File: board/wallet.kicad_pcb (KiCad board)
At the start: 4 copper layers, 48 x 85 mm, 136 parts, among them J1 TYPE-C-31-M-12, U1 BQ25185DLHR, U10 SN74LVC1T45DBVR, U11 E73-2G4M08S1C, U12 ME6211C28M5G-N, U13 TPS60230RGTR, U14 TLV75801PDBVR, U15 MAX17048G+T10, U2 TPS63802DLAR, U3 XC6206P332MR-G, U4 STM32U585VIT6Q, U5 SE050E2HQ1/Z01Z3Z, U6 TS3USB221ARSER, U7 SN74LVC1G02DBVR(UMW), U8 TPS22917DBVR, U9 SN74LVC1T45DBVR, Y1 Q13FC13500049

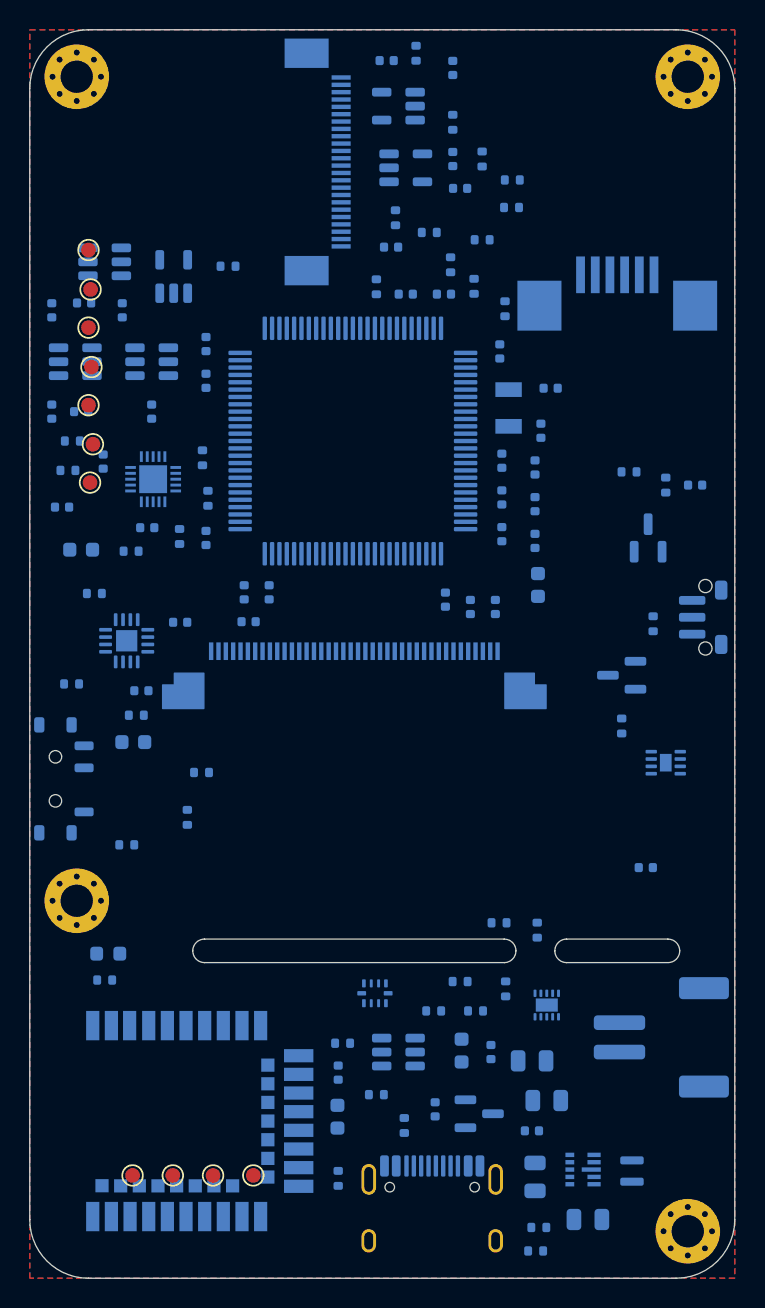
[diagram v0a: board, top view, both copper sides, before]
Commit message: Owner's hand placement and first routing
43 parts re-placed by hand (charger and buck-boost clusters tightened around
U1/U2 in the chin, battery gauge moved next to the MCU's I2C, decoupling and
crystal caps pulled in against their pins) and 38 nets routed: the power
chain, USB, display SPI, LSE, I2C, radio SWD, charger control.
310 track segments, 31 vias.

Co-Authored-By: Claude Opus 5.5 <noreply@anthropic.com>
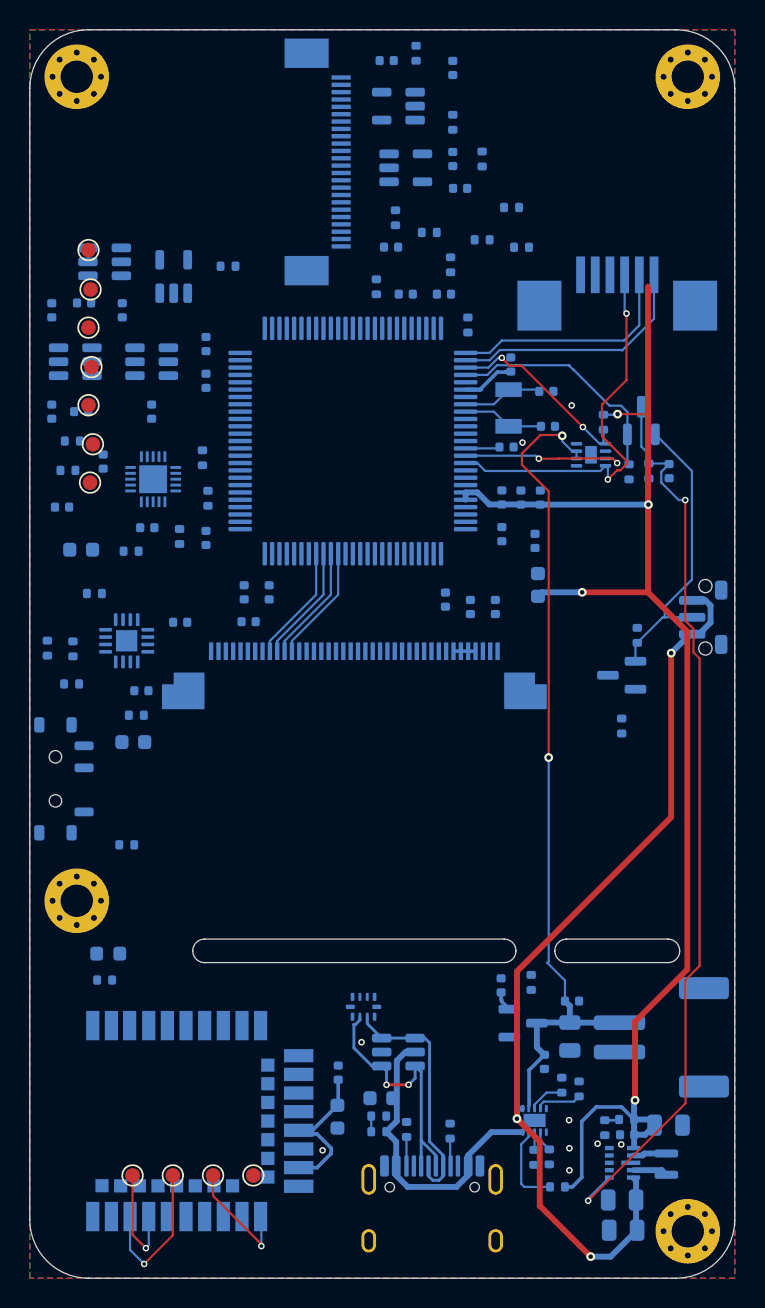
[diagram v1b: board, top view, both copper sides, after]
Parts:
- moved U15 21.6 mm to (38.2, 28.9)
- moved R_AIRS 15.0 mm to (1.20, 42.1)
- moved R_STAT1 14.6 mm to (35.9, 78.8), turned to 0 degrees
- moved R_ILIM 13.4 mm to (35.4, 76.7), turned to -90 degrees
- moved C_SYS 13.1 mm to (40.4, 81.7)
- moved R_ALRT 12.8 mm to (39.1, 26.7)
- moved R_CE 12.6 mm to (37.4, 72.1), turned to 90 degrees
- moved R_BLEN 12.1 mm to (2.94, 42.1), turned to 90 degrees
- moved C_USBSW 10.8 mm to (40.7, 75.2), turned to 180 degrees
- moved R_ISET 10.7 mm to (34.3, 76.8), turned to -90 degrees
- moved R_STAT2 10.7 mm to (36.2, 71.8)
- moved C_GAUGE 10.4 mm to (36.9, 66.1)
- moved C_RTC 10.1 mm to (32.1, 65.1), turned to 90 degrees
- moved R_FB2 9.62 mm to (39.1, 74.8), turned to -90 degrees
- moved R_FB1 9.47 mm to (40.6, 74.2), turned to 180 degrees
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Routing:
- net V3V3: track 0.00 -> 98.0 mm, vias 0 -> 4
- net PWR_EN: track 0.00 -> 62.5 mm, vias 0 -> 2
- net SYS: track 0.00 -> 62.1 mm, vias 0 -> 3
- net BAT: track 0.00 -> 57.5 mm, vias 0 -> 2
- net I2C_SDA: track 0.00 -> 26.9 mm, vias 0 -> 2
- net VBUS: track 0.00 -> 21.1 mm
- net BTN: track 0.00 -> 20.2 mm
- net USB_DP: track 0.00 -> 18.3 mm, vias 0 -> 2
- net USB_DN: track 0.00 -> 17.0 mm
- net CTP_INT: track 0.00 -> 17.0 mm
- net CTP_RST: track 0.00 -> 17.0 mm
- net PWR_HOLD: track 0.00 -> 16.2 mm
- net GAUGE_ALRT: track 0.00 -> 13.2 mm, vias 0 -> 2
- net I2C_SCL: track 0.00 -> 11.5 mm, vias 0 -> 2
- net RADIO_SWCLK: track 0.00 -> 10.5 mm, vias 0 -> 1
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
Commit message: Pre-route block wiring around the owner's routing; fix the stale MCU pin table
- board: block wiring (each IC and its passives) and GND fanouts routed with
  humanizedKicadAutoRouter on top of the owner's copper, which stays fixed;
  the USB pair from the MCU to the USB switch is routed first. The camera bus
  and VDD11's cross-package link are left to the human, like all wiring
  between blocks. 341/341 owner items and every footprint position unchanged;
  DRC has no new items, 10 of 12 starved thermals fixed. Autorouting the
  remainder as a judge: 2 failed nets (camera knot) vs 5 before.
- mcuAssign.json said USART1/PA9-PA10 for the radio but the netlist was never
  re-exported, so the board kept USART3/PB10-PB11. USART1 trial-routed worse
  (4 vs 2 failed), so the table now matches the board; checkMcuAf.py also
  fails when the table and the exported netlist disagree.
- scripts/partialRoute.py (new): partial routing with existing copper fixed,
  --first-nets, --skip-nets, --max-mm, --leave-under; removes its own
  dangling stubs.
- scripts/placeLoop.py (new): locked optimize -> partial route -> KRT judge.
- optimizePlacement: courtyards may touch, decap-to-pin cost, locked parts,
  clearance to existing copper. optimizePins: --keep-routed, --only, --out.
- checkDensity.py retired: the owner's placement packs courtyards touching.

Co-Authored-By: Claude Opus 5.5 <noreply@anthropic.com>
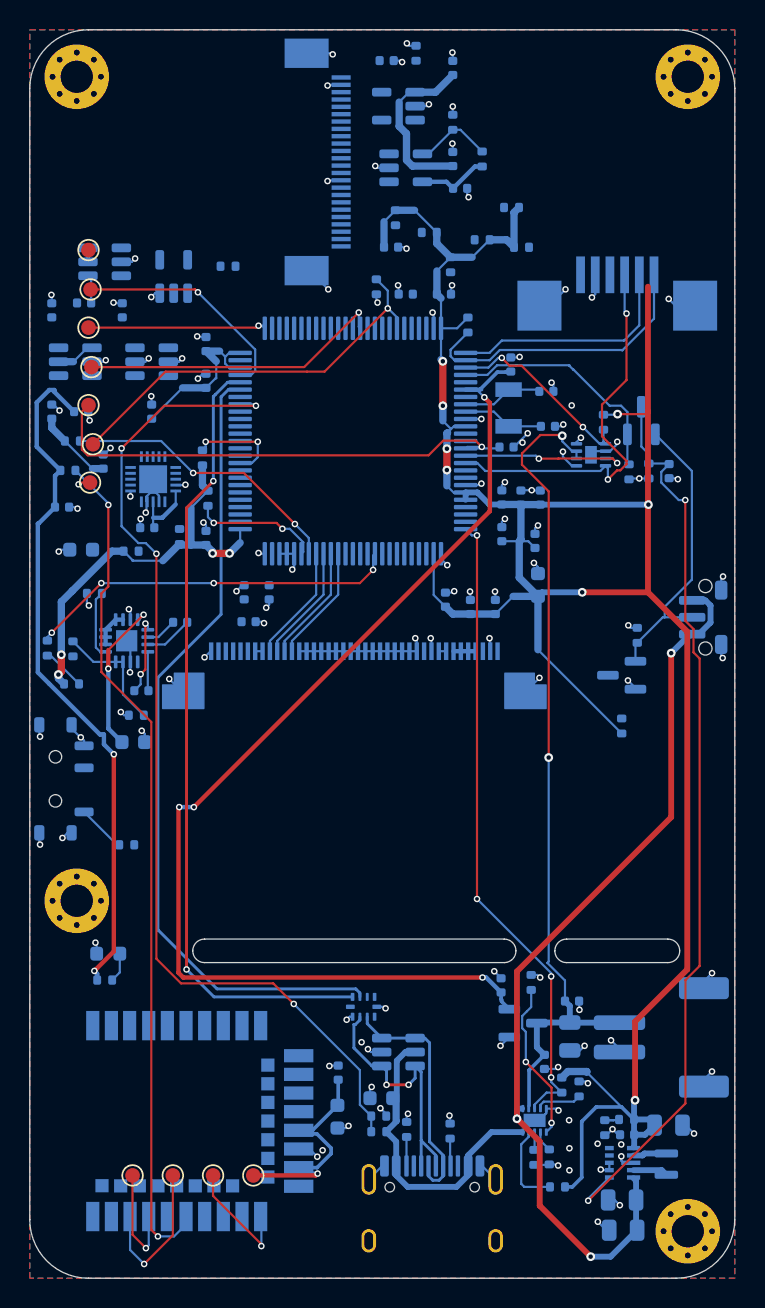
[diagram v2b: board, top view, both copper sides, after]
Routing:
- net V3V3: track 98.0 -> 236.9 mm, vias 4 -> 12
- net GND: track 0.00 -> 119.8 mm, vias 9 -> 123
- net VBAT_RTC: track 6.04 -> 78.7 mm, vias 0 -> 4
- net VBUS_SENSE: track 1.06 -> 69.0 mm, vias 0 -> 4
- net RADIO_TX: track 0.00 -> 57.7 mm, vias 0 -> 2
- net USB_DN_MCU: track 0.00 -> 55.4 mm
- net USB_DP_MCU: track 0.00 -> 54.1 mm, vias 0 -> 2
- net RADIO_3V3: track 10.1 -> 64.1 mm, vias 0 -> 3
- net CHG_STAT2: track 2.71 -> 44.0 mm, vias 0 -> 4
- net NRST: track 2.34 -> 34.7 mm, vias 0 -> 1
- net BOOT0: track 0.00 -> 27.8 mm, vias 0 -> 1
- net AIRGAP_SENSE: track 0.00 -> 25.5 mm, vias 0 -> 4
- net SWO: track 0.00 -> 20.9 mm, vias 0 -> 1
- net RADIO_TXD_MCU: track 0.00 -> 19.4 mm, vias 0 -> 2
- net SWDIO: track 0.00 -> 15.5 mm, vias 0 -> 1
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
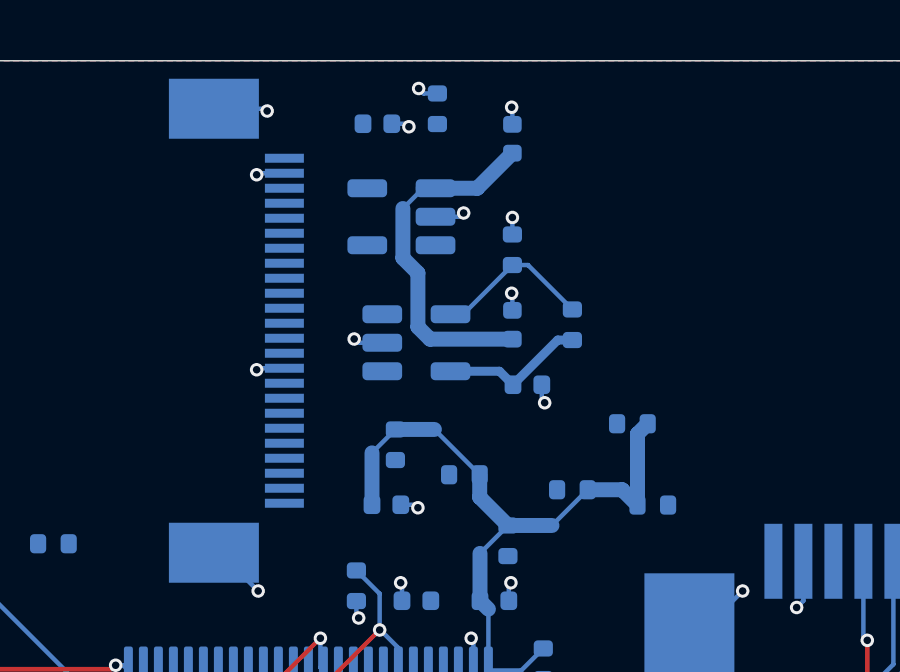
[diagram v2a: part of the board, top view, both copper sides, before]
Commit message: Owner's fixes on the pre-routed board (checkpoint before rework)
Co-Authored-By: Claude Opus 5.5 <noreply@anthropic.com>
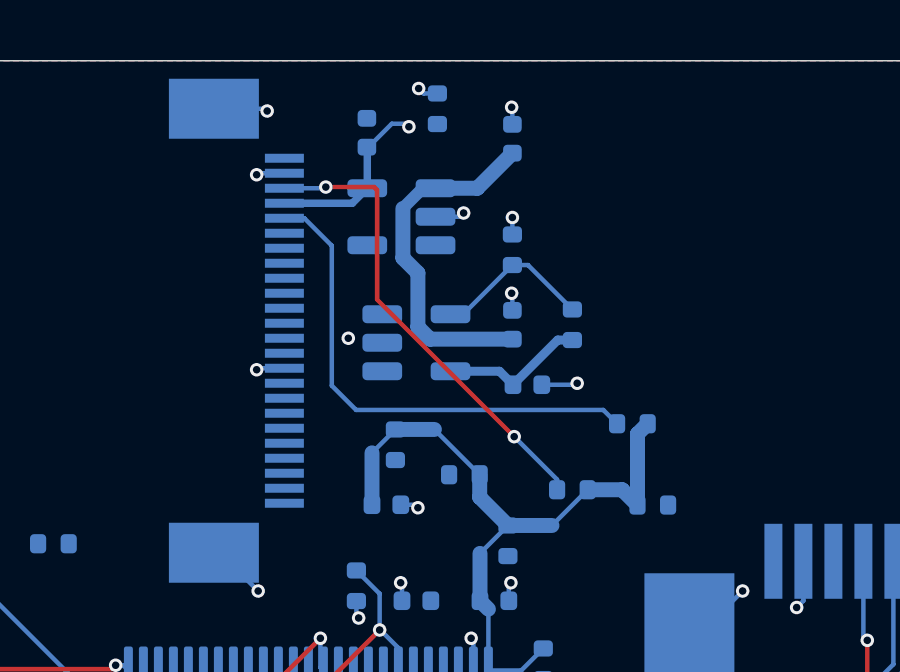
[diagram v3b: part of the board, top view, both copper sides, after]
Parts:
- moved C_AVOUT 0.46 mm to (23.9, 2.40), turned to 90 degrees
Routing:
- net CAM_SCL: track 0.00 -> 16.7 mm
- net CAM_SDA: track 0.00 -> 15.6 mm, vias 0 -> 2
- net CAM_AVDD: track 0.00 -> 6.11 mm, vias 0 -> 1
- net GND: track 119.8 -> 118.8 mm, vias 123 -> 122
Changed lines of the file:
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@@
 	(footprint "Capacitor_SMD:C_0402_1005Metric"
 		(layer "B.Cu")
-		(at 24.3 2.099999)
+		(at 23.95 2.4 90)
 		(descr "Capacitor SMD 0402 (1005 Metric), square (rectangular) end terminal, IPC-7351 nominal, (Body size source: IPC-SM-782 page 76, https://www.pcb-3d.com/wordpress/wp-content/uploads/ipc-sm-782a_amendment_1_and_2.pdf)")
 		(tags "capacitor")
 		(property "Reference" "C_AVOUT"
-			(at 0 0 180)
+			(at 0 0 90)
 			(layer "B.Fab")
 			(effects
@@
 		)
 		(property "Value" "1uF"
-			(at 0 -1.16 180)
+			(at 0 -1.16 90)
 			(layer "B.Fab")
 			(hide yes)
@@
 		)
 		(property "Datasheet" ""
-			(at 0 0 180)
+			(at 0 0 90)
 			(layer "B.Fab")
 			(hide yes)
@@
 		)
 		(property "Description" ""
-			(at 0 0 180)
+			(at 0 0 90)
 			(layer "B.Fab")
 			(hide yes)
@@
 		)
 		(property "KiLib_Generator" "SMD_2terminal_chip_molded"
-			(at 0 0 180)
+			(at 0 0 90)
 			(layer "B.SilkS")
 			(hide yes)
@@
 		)
 		(property "LCSC" "C52923"
-			(at 0 0 180)
+			(at 0 0 90)
 			(layer "B.Fab")
 			(hide yes)
@@
 		)
 		(fp_text user "${REFERENCE}"
-			(at 0 0 180)
+			(at 0 0 90)
 			(layer "B.Fab")
 			(effects
@@
 		)
 		(pad "1" smd roundrect
-			(at -0.48 0)
+			(at -0.48 0 90)
 			(size 0.56 0.62)
 			(layers "B.Cu" "B.Mask" "B.Paste")
@@
 		)
 		(pad "2" smd roundrect
-			(at 0.48 0)
+			(at 0.48 0 90)
 			(size 0.56 0.62)
 			(layers "B.Cu" "B.Mask" "B.Paste")
@@
 	)
 	(via
-		(at 25.35 2.2)
-		(size 0.45)
-		(drill 0.25)
-		(layers "F.Cu" "B.Cu")
-		(net "GND")
-	)
-	(via
 		(at 4.475 62.15)
 		(size 0.45)
@@
 	)
 	(via
-		(at 29.875 11.4)
+		(at 30.96 10.75)
 		(size 0.45)
 		(drill 0.25)
@@
 	)
 	(via
+		(at 23.33 9.25)
+		(size 0.45)
+		(drill 0.25)
+		(layers "F.Cu" "B.Cu")
+		(free yes)
+		(net "GND")
+	)
+	(via
 		(at 40.27 75.89)
 		(size 0.45)
@@
 	)
 	(via
-		(at 23.525 9.275)
-		(size 0.45)
-		(drill 0.25)
-		(layers "F.Cu" "B.Cu")
-		(net "GND")
-	)
-	(via
 		(at 8.275 24.95)
 		(size 0.45)
@@
 	)
 	(segment
-		(start 24.4625 9.4)
-		(end 23.65 9.4)
-		(width 0.15)
-		(layer "B.Cu")
-		(net "GND")
-	)
-	(segment
 		(start 38.21 28.94)
 		(end 38.46 28.69)
@@
 	)
 	(segment
+		(start 30.91 10.8)
+		(end 30.96 10.75)
+		(width 0.15)
+		(layer "B.Cu")
+		(net "GND")
+	)
+	(segment
 		(start 12 34.12)
 		(end 12 33.725)
@@
 	)
 	(segment
-		(start 29.78 10.8)
-		(end 29.78 11.305)
-		(width 0.15)
-		(layer "B.Cu")
-		(net "GND")
-	)
-	(segment
 		(start 3.7 48.4)
 		(end 3.475 48.175)
@@
 	)
 	(segment
-		(start 24.78 2.099999)
-		(end 25.249999 2.099999)
-		(width 0.15)
-		(layer "B.Cu")
-		(net "GND")
-	)
-	(segment
 		(start 40.15 69.6)
 		(end 40.15 69.375)
@@
 	)
 	(segment
-		(start 29.78 11.305)
-		(end 29.875 11.4)
-		(width 0.15)
-		(layer "B.Cu")
-		(net "GND")
-	)
-	(segment
 		(start 35.17 73.45)
 		(end 35.875 73.45)
@@
 	)
 	(segment
+		(start 29.78 10.8)
+		(end 30.91 10.8)
+		(width 0.15)
+		(layer "B.Cu")
+		(net "GND")
+	)
+	(segment
 		(start 21.85 42.309999)
 		(end 22.35 42.309999)
@@
 	)
 	(segment
-		(start 25.249999 2.099999)
-		(end 25.35 2.2)
-		(width 0.15)
-		(layer "B.Cu")
-		(net "GND")
-	)
-	(segment
 		(start 35.34 77.28)
 		(end 35.37 77.25)
@@
 	)
 	(segment
-		(start 23.65 9.4)
-		(end 23.525 9.275)
-		(width 0.15)
-		(layer "B.Cu")
-		(net "GND")
-	)
-	(segment
 		(start 25.66 73.89)
 		(end 25.75 73.8)
@@
 	)
 	(segment
+		(start 25.15 4.913738)
+		(end 25.15 4.925)
+		(width 0.4)
+		(layer "B.Cu")
+		(net "V3V3")
+	)
+	(segment
 		(start 12.93 21.88)
 		(end 13.3 22.25)
@@
 	)
 	(segment
+		(start 25.813738 4.25)
+		(end 25.15 4.913738)
+		(width 0.4)
+		(layer "B.Cu")
+		(net "V3V3")
+	)
+	(segment
 		(start 28.3 39.28)
 		(end 27.5 38.48)
@@
 	)
 	(segment
+		(start 25.825 4.25)
+		(end 25.813738 4.25)
+		(width 0.4)
+		(layer "B.Cu")
+		(net "V3V3")
+	)
+	(segment
 		(start 4.27 29.88)
 		(end 5 29.88)
@@
 	)
 	(segment
-		(start 25.15 4.925)
-		(end 25.825 4.25)
-		(width 0.15)
-		(layer "B.Cu")
-		(net "V3V3")
-	)
-	(segment
 		(start 41.14 74.19)
 		(end 41.14 75.22)
@@
 		(net "BTN")
 	)
+	(via
+		(at 25.35 2.2)
+		(size 0.45)
+		(drill 0.25)
+		(layers "F.Cu" "B.Cu")
+		(net "CAM_AVDD")
+	)
+	(segment
+		(start 24.78 2.099999)
+		(end 23.999999 2.88)
+		(width 0.15)
+		(layer "B.Cu")
+		(net "CAM_AVDD")
+	)
+	(segment
+		(start 24.78 2.099999)
+		(end 25.249999 2.099999)
+		(width 0.15)
+		(layer "B.Cu")
+		(net "CAM_AVDD")
+	)
+	(segment
+		(start 23.999999 2.88)
+		(end 23.95 2.88)
+		(width 0.15)
+		(layer "B.Cu")
+		(net "CAM_AVDD")
+	)
+	(segment
+		(start 21.2 4.75)
+		(end 23.4625 4.75)
+		(width 0.25)
+		(layer "B.Cu")
+		(net "CAM_AVDD")
+	)
+	(segment
+		(start 25.249999 2.099999)
+		(end 25.35 2.2)
+		(width 0.15)
+		(layer "B.Cu")
+		(net "CAM_AVDD")
+	)
+	(segment
+		(start 23.4625 4.75)
+		(end 23.9625 4.25)
+		(width 0.25)
+		(layer "B.Cu")
+		(net "CAM_AVDD")
+	)
+	(segment
+		(start 23.9625 4.25)
+		(end 23.9625 2.8925)
+		(width 0.25)
+		(layer "B.Cu")
+		(net "CAM_AVDD")
+	)
+	(segment
+		(start 23.9625 2.8925)
+		(end 23.95 2.88)
+		(width 0.25)
+		(layer "B.Cu")
+		(net "CAM_AVDD")
+	)
 	(segment
 		(start 45.605 42.80396)
@@
 	)
 	(segment
+		(start 31.829999 11.64)
+		(end 32.289999 12.1)
+		(width 0.15)
+		(layer "B.Cu")
+		(net "CAM_SCL")
+	)
+	(segment
+		(start 22.78 10.83)
+		(end 23.59 11.64)
+		(width 0.15)
+		(layer "B.Cu")
+		(net "CAM_SCL")
+	)
+	(segment
+		(start 21.865514 5.25)
+		(end 22.78 6.164486)
+		(width 0.15)
+		(layer "B.Cu")
+		(net "CAM_SCL")
+	)
+	(segment
+		(start 22.78 6.164486)
+		(end 22.78 10.83)
+		(width 0.15)
+		(layer "B.Cu")
+		(net "CAM_SCL")
+	)
+	(segment
+		(start 23.59 11.64)
+		(end 31.829999 11.64)
+		(width 0.15)
+		(layer "B.Cu")
+		(net "CAM_SCL")
+	)
+	(segment
+		(start 21.2 5.25)
+		(end 21.865514 5.25)
+		(width 0.15)
+		(layer "B.Cu")
+		(net "CAM_SCL")
+	)
+	(segment
+		(start 24.19 4.21)
+		(end 24.29 4.31)
+		(width 0.15)
+		(layer "F.Cu")
+		(net "CAM_SDA")
+	)
+	(segment
+		(start 24.29 4.31)
+		(end 24.29 7.96)
+		(width 0.15)
+		(layer "F.Cu")
+		(net "CAM_SDA")
+	)
+	(segment
+		(start 22.58 4.21)
+		(end 24.19 4.21)
+		(width 0.15)
+		(layer "F.Cu")
+		(net "CAM_SDA")
+	)
+	(segment
+		(start 24.29 7.96)
+		(end 28.86 12.53)
+		(width 0.15)
+		(layer "F.Cu")
+		(net "CAM_SDA")
+	)
+	(via
+		(at 28.86 12.53)
+		(size 0.45)
+		(drill 0.25)
+		(layers "F.Cu" "B.Cu")
+		(net "CAM_SDA")
+	)
+	(via
+		(at 22.58 4.21)
+		(size 0.45)
+		(drill 0.25)
+		(layers "F.Cu" "B.Cu")
+		(net "CAM_SDA")
+	)
+	(segment
+		(start 28.86 12.53)
+		(end 30.289999 13.959999)
+		(width 0.15)
+		(layer "B.Cu")
+		(net "CAM_SDA")
+	)
+	(segment
+		(start 22.54 4.25)
+		(end 22.58 4.21)
+		(width 0.15)
+		(layer "B.Cu")
+		(net "CAM_SDA")
+	)
+	(segment
+		(start 30.289999 13.959999)
+		(end 30.289999 14.3)
+		(width 0.15)
+		(layer "B.Cu")
+		(net "CAM_SDA")
+	)
+	(segment
+		(start 21.2 4.25)
+		(end 22.54 4.25)
+		(width 0.15)
+		(layer "B.Cu")
+		(net "CAM_SDA")
+	)
+	(segment
